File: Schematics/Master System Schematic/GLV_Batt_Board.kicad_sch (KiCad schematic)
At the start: 0 parts

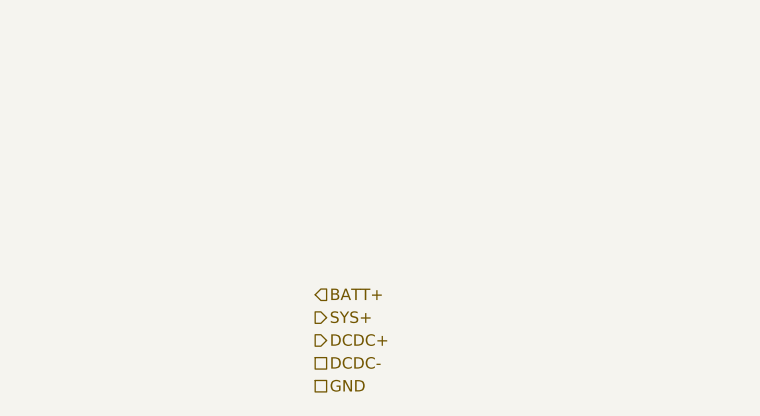
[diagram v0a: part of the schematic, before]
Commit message: Initial LV 2023 Competition Update
List of questions/comments: https://docs.google.com/document/d/1Jezx0FskMhwUdHdk8isXV7eDmPDUZPOb6vodgO5P4QI/edit?usp=sharing
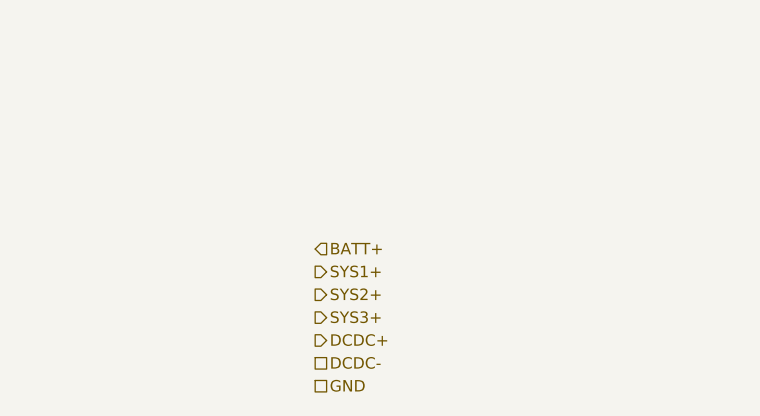
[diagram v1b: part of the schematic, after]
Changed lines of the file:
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@@
     (effects (font (size 3.9878 3.9878)) (justify left bottom))
   )
-  (hierarchical_label "BATT+" (shape input) (at 93.98 93.98 0)
+  (hierarchical_label "BATT+" (shape input) (at 93.98 88.9 0)
     (effects (font (size 1.27 1.27)) (justify left))
   )
-  (hierarchical_label "SYS+" (shape output) (at 93.98 96.52 0)
+  (hierarchical_label "SYS3+" (shape output) (at 93.98 96.52 0)
     (effects (font (size 1.27 1.27)) (justify left))
   )
   (hierarchical_label "DCDC-" (shape passive) (at 93.98 101.6 0)
+    (effects (font (size 1.27 1.27)) (justify left))
+  )
+  (hierarchical_label "SYS2+" (shape output) (at 93.98 93.98 0)
     (effects (font (size 1.27 1.27)) (justify left))
   )
@@
     (effects (font (size 1.27 1.27)) (justify left))
   )
+  (hierarchical_label "SYS1+" (shape output) (at 93.98 91.44 0)
+    (effects (font (size 1.27 1.27)) (justify left))
+  )

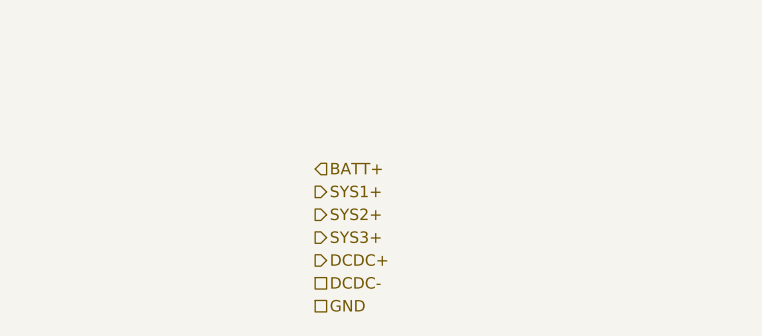
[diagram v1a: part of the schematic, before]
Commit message: Upgraded to kicad 7 and fixed dcdc
Upgraded to kicad 7
added triple-wire runs to dcdc lines
added inline fuses and glvms switch for dcdc
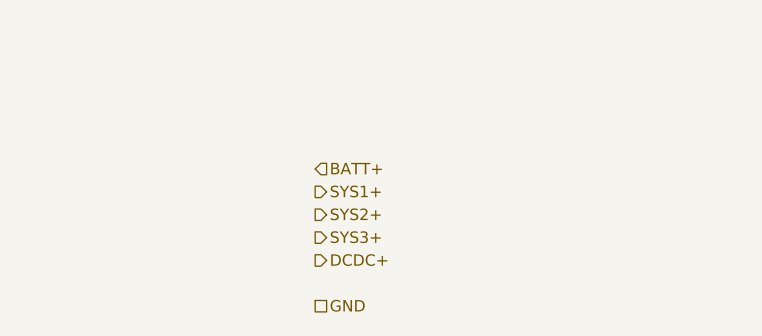
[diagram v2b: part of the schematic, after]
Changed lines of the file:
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@@
-(kicad_sch (version 20211123) (generator eeschema)
+(kicad_sch (version 20230121) (generator eeschema)
   (paper "A")
   (title_block
@@
     (effects (font (size 3.9878 3.9878)) (justify left bottom))
   )
-  (hierarchical_label "BATT+" (shape input) (at 93.98 88.9 0)
+  (hierarchical_label "BATT+" (shape input) (at 93.98 88.9 0) (fields_autoplaced)
     (effects (font (size 1.27 1.27)) (justify left))
   )
-  (hierarchical_label "SYS3+" (shape output) (at 93.98 96.52 0)
+  (hierarchical_label "SYS3+" (shape output) (at 93.98 96.52 0) (fields_autoplaced)
     (effects (font (size 1.27 1.27)) (justify left))
   )
-  (hierarchical_label "DCDC-" (shape passive) (at 93.98 101.6 0)
+  (hierarchical_label "SYS2+" (shape output) (at 93.98 93.98 0) (fields_autoplaced)
     (effects (font (size 1.27 1.27)) (justify left))
   )
-  (hierarchical_label "SYS2+" (shape output) (at 93.98 93.98 0)
+  (hierarchical_label "CAN_L" (shape bidirectional) (at 157.48 95.25 0) (fields_autoplaced)
     (effects (font (size 1.27 1.27)) (justify left))
   )
-  (hierarchical_label "CAN_L" (shape bidirectional) (at 157.48 95.25 0)
+  (hierarchical_label "CAN_S" (shape passive) (at 157.48 100.33 0) (fields_autoplaced)
     (effects (font (size 1.27 1.27)) (justify left))
   )
-  (hierarchical_label "CAN_S" (shape passive) (at 157.48 100.33 0)
+  (hierarchical_label "SYS1+" (shape output) (at 93.98 91.44 0) (fields_autoplaced)
     (effects (font (size 1.27 1.27)) (justify left))
   )
-  (hierarchical_label "SYS1+" (shape output) (at 93.98 91.44 0)
+  (hierarchical_label "DCDC+" (shape output) (at 93.98 99.06 0) (fields_autoplaced)
     (effects (font (size 1.27 1.27)) (justify left))
   )
-  (hierarchical_label "DCDC+" (shape output) (at 93.98 99.06 0)
+  (hierarchical_label "GND" (shape passive) (at 93.98 104.14 0) (fields_autoplaced)
     (effects (font (size 1.27 1.27)) (justify left))
   )
-  (hierarchical_label "GND" (shape passive) (at 93.98 104.14 0)
+  (hierarchical_label "CAN_H" (shape bidirectional) (at 157.48 97.79 0) (fields_autoplaced)
     (effects (font (size 1.27 1.27)) (justify left))
   )
-  (hierarchical_label "CAN_H" (shape bidirectional) (at 157.48 97.79 0)
-    (effects (font (size 1.27 1.27)) (justify left))
-  )

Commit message: Addressed review feedback
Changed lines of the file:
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@@
     (comment 2 "For authors and other info, contact Chief Electrical Engineer")
+  )
+  (junction (at 90.17 93.98) (diameter 0) (color 0 0 0 0)
+  )
+  (wire (pts (xy 90.17 93.98) (xy 93.98 93.98))
+    (stroke (width 0) (type default))
+  )
+  (wire (pts (xy 90.17 96.52) (xy 93.98 96.52))
+    (stroke (width 0) (type default))
+  )
+  (wire (pts (xy 93.98 91.44) (xy 90.17 91.44))
+    (stroke (width 0) (type default))
+  )
+  (wire (pts (xy 90.17 93.98) (xy 90.17 96.52))
+    (stroke (width 0) (type default))
+  )
+  (wire (pts (xy 90.17 91.44) (xy 90.17 93.98))
+    (stroke (width 0) (type default))
   )
   (text "SEE ALTIUM SCHEMATIC FOR FINAL IMPLEMENTATION" (at 60.96 25.4 0)
@@
     (effects (font (size 1.27 1.27)) (justify left))
   )
+  (hierarchical_label "PDU_GND3" (shape passive) (at 93.98 111.76 0) (fields_autoplaced)
+    (effects (font (size 1.27 1.27)) (justify left))
+  )
   (hierarchical_label "SYS2+" (shape output) (at 93.98 93.98 0) (fields_autoplaced)
+    (effects (font (size 1.27 1.27)) (justify left))
+  )
+  (hierarchical_label "PDU_GND1" (shape passive) (at 93.98 106.68 0) (fields_autoplaced)
     (effects (font (size 1.27 1.27)) (justify left))
   )
@@
     (effects (font (size 1.27 1.27)) (justify left))
   )
+  (hierarchical_label "PDU_GND2" (shape passive) (at 93.98 109.22 0) (fields_autoplaced)
+    (effects (font (size 1.27 1.27)) (justify left))
+  )

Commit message: Matt changes - WIP
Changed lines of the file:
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@@
     (comment 2 "For authors and other info, contact Chief Electrical Engineer")
   )
+  (junction (at 90.17 101.6) (diameter 0) (color 0 0 0 0)
+  )
   (junction (at 90.17 93.98) (diameter 0) (color 0 0 0 0)
+  )
+  (wire (pts (xy 93.98 99.06) (xy 90.17 99.06))
+    (stroke (width 0) (type default))
   )
   (wire (pts (xy 90.17 93.98) (xy 93.98 93.98))
     (stroke (width 0) (type default))
   )
+  (wire (pts (xy 90.17 101.6) (xy 93.98 101.6))
+    (stroke (width 0) (type default))
+  )
   (wire (pts (xy 90.17 96.52) (xy 93.98 96.52))
+    (stroke (width 0) (type default))
+  )
+  (wire (pts (xy 90.17 104.14) (xy 90.17 101.6))
     (stroke (width 0) (type default))
   )
@@
     (stroke (width 0) (type default))
   )
+  (wire (pts (xy 93.98 104.14) (xy 90.17 104.14))
+    (stroke (width 0) (type default))
+  )
+  (wire (pts (xy 90.17 99.06) (xy 90.17 101.6))
+    (stroke (width 0) (type default))
+  )
   (text "SEE ALTIUM SCHEMATIC FOR FINAL IMPLEMENTATION" (at 60.96 25.4 0)
     (effects (font (size 3.9878 3.9878)) (justify left bottom))
@@
     (effects (font (size 1.27 1.27)) (justify left))
   )
-  (hierarchical_label "PDU_GND3" (shape passive) (at 93.98 111.76 0) (fields_autoplaced)
+  (hierarchical_label "PDU_GND3" (shape passive) (at 93.98 124.46 0) (fields_autoplaced)
+    (effects (font (size 1.27 1.27)) (justify left))
+  )
+  (hierarchical_label "DCDC2" (shape input) (at 93.98 101.6 0) (fields_autoplaced)
     (effects (font (size 1.27 1.27)) (justify left))
   )
@@
     (effects (font (size 1.27 1.27)) (justify left))
   )
-  (hierarchical_label "PDU_GND1" (shape passive) (at 93.98 106.68 0) (fields_autoplaced)
+  (hierarchical_label "PDU_GND1" (shape passive) (at 93.98 119.38 0) (fields_autoplaced)
+    (effects (font (size 1.27 1.27)) (justify left))
+  )
+  (hierarchical_label "DCDC3" (shape input) (at 93.98 104.14 0) (fields_autoplaced)
     (effects (font (size 1.27 1.27)) (justify left))
   )
@@
     (effects (font (size 1.27 1.27)) (justify left))
   )
-  (hierarchical_label "DCDC+" (shape output) (at 93.98 99.06 0) (fields_autoplaced)
+  (hierarchical_label "DCDC1" (shape input) (at 93.98 99.06 0) (fields_autoplaced)
     (effects (font (size 1.27 1.27)) (justify left))
   )
-  (hierarchical_label "GND" (shape passive) (at 93.98 104.14 0) (fields_autoplaced)
+  (hierarchical_label "GND" (shape passive) (at 93.98 116.84 0) (fields_autoplaced)
     (effects (font (size 1.27 1.27)) (justify left))
   )
@@
     (effects (font (size 1.27 1.27)) (justify left))
   )
-  (hierarchical_label "PDU_GND2" (shape passive) (at 93.98 109.22 0) (fields_autoplaced)
+  (hierarchical_label "PDU_GND2" (shape passive) (at 93.98 121.92 0) (fields_autoplaced)
     (effects (font (size 1.27 1.27)) (justify left))
   )
